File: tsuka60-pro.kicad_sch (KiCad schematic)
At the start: 166 parts, among them J1 USB_C_Receptacle_USB2.0, J2 Conn_01x04_MountingPin, SW1 SW_Reset, U1 ATmega32U4-M, U2 SRV05-4, Y1 16MHz

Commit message: Made important changes to the keyboard, re-exported production files
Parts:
- added MX70_2: MX-NoLED, marbastlib-mx:SW_MX_HS_1u, symbol MX_Alps_Hybrid:MX-NoLED
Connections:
- net COL9: now also MX70.1 (COL), MX70_2.1 (COL)
- net 70_2: now reaches D70.2 (A), MX70.2 (ROW)
- net 70_2: now also MX70_2.2 (ROW)
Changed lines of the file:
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@@
   (junction (at 166.37 138.43) (diameter 0) (color 0 0 0 0)
   )
+  (junction (at 171.45 166.37) (diameter 0) (color 0 0 0 0)
+  )
   (junction (at 82.55 90.17) (diameter 0) (color 0 0 0 0)
   )
@@
     (stroke (width 0) (type default) (color 0 0 0 0))
   )
+  (wire (pts (xy 171.45 166.37) (xy 171.45 204.47))
+    (stroke (width 0) (type default) (color 0 0 0 0))
+  )
   (wire (pts (xy 102.87 62.23) (xy 90.17 62.23))
     (stroke (width 0) (type default) (color 0 0 0 0))
@@
     )
   )
+  (global_label "70_2" (shape input) (at 179.07 260.35 180) (fields_autoplaced)
+    (effects (font (size 1.27 1.27)) (justify right))
+    (property "Intersheet References" "${INTERSHEET_REFS}" (id 0) (at 172.0607 260.2706 0)
+      (effects (font (size 1.27 1.27)) (justify right) hide)
+    )
+  )
   (global_label "COL11" (shape input) (at 370.84 53.34 0) (fields_autoplaced)
     (effects (font (size 1.27 1.27)) (justify left))
@@
     )
   )
+  (global_label "70_2" (shape input) (at 166.37 209.55 180) (fields_autoplaced)
+    (effects (font (size 1.27 1.27)) (justify right))
+    (property "Intersheet References" "${INTERSHEET_REFS}" (id 0) (at 159.3607 209.4706 0)
+      (effects (font (size 1.27 1.27)) (justify right) hide)
+    )
+  )
   (global_label "COL6" (shape input) (at 370.84 73.66 0) (fields_autoplaced)
     (effects (font (size 1.27 1.27)) (justify left))
@@
     )
   )
+  (global_label "COL9" (shape input) (at 184.15 255.27 270) (fields_autoplaced)
+    (effects (font (size 1.27 1.27)) (justify right))
+    (property "Intersheet References" "${INTERSHEET_REFS}" (id 0) (at 184.0706 262.5212 90)
+      (effects (font (size 1.27 1.27)) (justify right) hide)
+    )
+  )
   (global_label "XTAL1" (shape input) (at 304.8 76.2 0) (fields_autoplaced)
     (effects (font (size 1.27 1.27)) (justify left))
@@
     (pin "2")
   )
+  (symbol (lib_id "MX_Alps_Hybrid:MX-NoLED") (at 180.34 256.54 0) (unit 1)
+    (in_bom yes) (on_board yes) (fields_autoplaced)
+    (property "Reference" "MX70_2" (id 0) (at 181.2256 250.19 0)
+      (effects (font (size 1.524 1.524)))
+    )
+    (property "Value" "MX-NoLED" (id 1) (at 181.2256 251.46 0)
+      (effects (font (size 0.508 0.508)))
+    )
+    (property "Footprint" "marbastlib-mx:SW_MX_HS_1u" (id 2) (at 164.465 257.175 0)
+      (effects (font (size 1.524 1.524)) hide)
+    )
+    (property "Datasheet" "" (id 3) (at 164.465 257.175 0)
+      (effects (font (size 1.524 1.524)) hide)
+    )
+    (pin "1")
+    (pin "2")
+  )
   (symbol (lib_id "Device:D_Small") (at 77.47 212.09 90) (unit 1)
     (in_bom yes) (on_board yes)
@@
       (reference "MX70") (unit 1) (value "MX-NoLED") (footprint "marbastlib-mx:SW_MX_HS_1.25u")
     )
+    (path "/834bb16e-2315-416c-95af-99912f2fa973"
+      (reference "MX70_2") (unit 1) (value "MX-NoLED") (footprint "marbastlib-mx:SW_MX_HS_1u")
+    )
     (path "/2db2779d-a5fd-464e-b5ae-8e46bd29d16e"

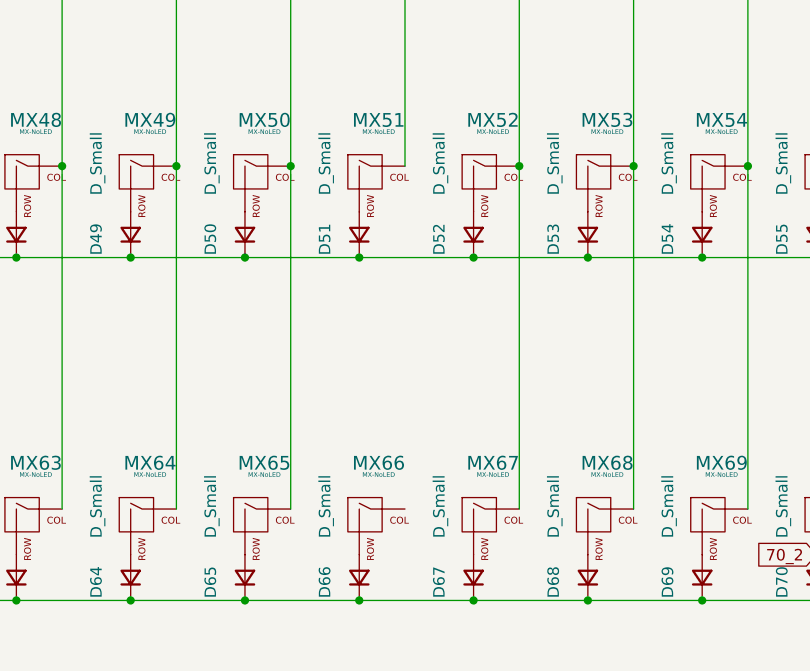
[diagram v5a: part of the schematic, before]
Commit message: Add missing trace
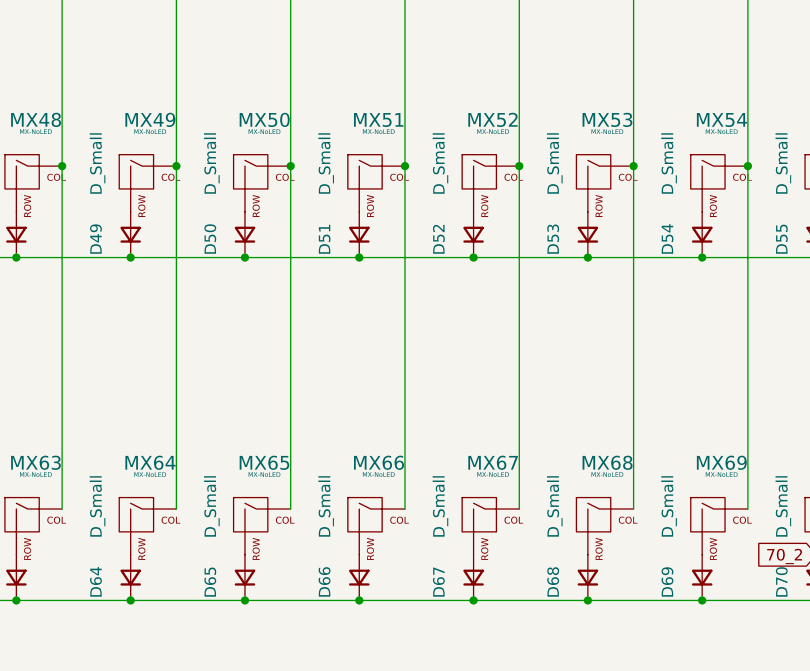
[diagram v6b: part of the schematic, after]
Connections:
- net COL5: now also MX66.1 (COL)
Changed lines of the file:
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@@
   (junction (at 289.56 85.09) (diameter 0) (color 0 0 0 0)
+  )
+  (junction (at 120.65 166.37) (diameter 0) (color 0 0 0 0)
   )
   (junction (at 115.57 176.53) (diameter 0) (color 0 0 0 0)
@@
     (stroke (width 0) (type default) (color 0 0 0 0))
   )
+  (wire (pts (xy 120.65 166.37) (xy 120.65 204.47))
+    (stroke (width 0) (type default) (color 0 0 0 0))
+  )

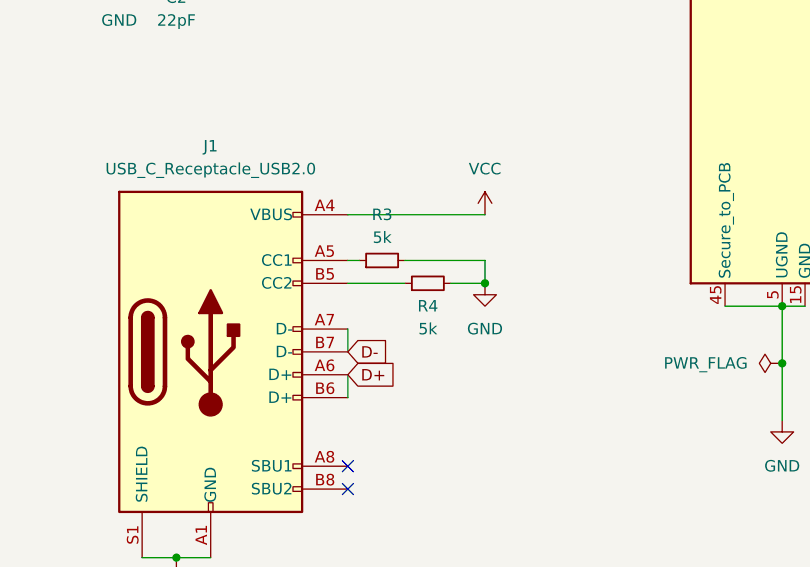
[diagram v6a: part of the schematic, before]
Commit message: Repair BOM, update USB-C component, footprint and placement
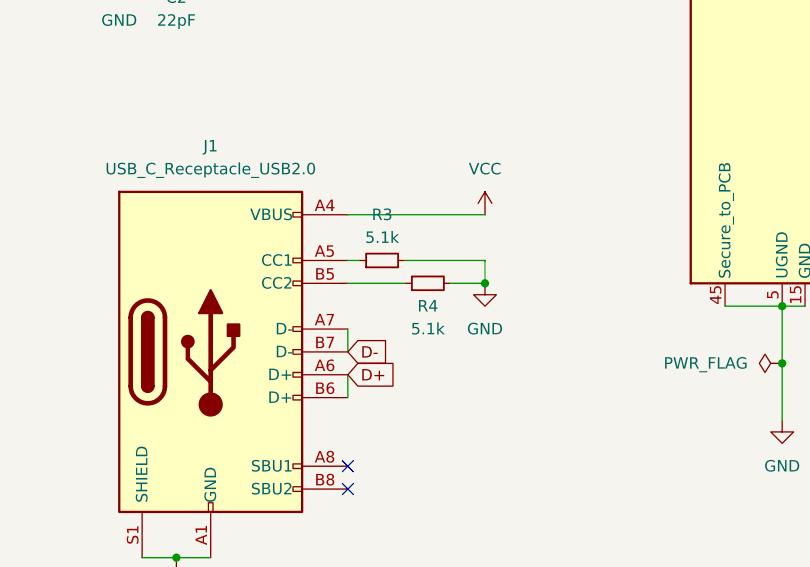
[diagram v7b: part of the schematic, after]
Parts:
- J1: footprint marbastlib-various:USB_C_Receptacle_HRO_TYPE-C-31-M-14 -> Connector_USB:USB_C_Receptacle_HRO_TYPE-C-31-M-12
- R3, R4: value 5k -> 5.1k
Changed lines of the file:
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@@
     (property "Reference" "J1" (id 0) (at 289.56 109.22 0))
     (property "Value" "USB_C_Receptacle_USB2.0" (id 1) (at 289.56 111.76 0))
-    (property "Footprint" "marbastlib-various:USB_C_Receptacle_HRO_TYPE-C-31-M-14" (id 2) (at 293.37 132.08 0)
+    (property "Footprint" "Connector_USB:USB_C_Receptacle_HRO_TYPE-C-31-M-12" (id 2) (at 293.37 132.08 0)
       (effects (font (size 1.27 1.27)) hide)
     )
@@
     (in_bom yes) (on_board yes)
     (property "Reference" "R4" (id 0) (at 313.69 127 90))
-    (property "Value" "5k" (id 1) (at 313.69 129.54 90))
+    (property "Value" "5.1k" (id 1) (at 313.69 129.54 90))
     (property "Footprint" "Capacitor_SMD:C_0603_1608Metric_Pad1.08x0.95mm_HandSolder" (id 2) (at 313.69 124.46 0)
       (effects (font (size 1.27 1.27)) hide)
@@
     (in_bom yes) (on_board yes)
     (property "Reference" "R3" (id 0) (at 308.61 116.84 90))
-    (property "Value" "5k" (id 1) (at 308.61 119.38 90))
+    (property "Value" "5.1k" (id 1) (at 308.61 119.38 90))
     (property "Footprint" "Capacitor_SMD:C_0603_1608Metric_Pad1.08x0.95mm_HandSolder" (id 2) (at 308.61 121.92 0)
       (effects (font (size 1.27 1.27)) hide)
@@
     )
     (path "/39fd6eec-df64-4ec7-90d9-dff965db8c15"
-      (reference "J1") (unit 1) (value "USB_C_Receptacle_USB2.0") (footprint "marbastlib-various:USB_C_Receptacle_HRO_TYPE-C-31-M-14")
+      (reference "J1") (unit 1) (value "USB_C_Receptacle_USB2.0") (footprint "Connector_USB:USB_C_Receptacle_HRO_TYPE-C-31-M-12")
     )
     (path "/08e6d373-2bf3-4f1e-87e0-beb65fb65c5f"
@@
     )
     (path "/65a31d27-e55c-4cca-9abe-ecfeb4877455"
-      (reference "R3") (unit 1) (value "5k") (footprint "Capacitor_SMD:C_0603_1608Metric_Pad1.08x0.95mm_HandSolder")
+      (reference "R3") (unit 1) (value "5.1k") (footprint "Capacitor_SMD:C_0603_1608Metric_Pad1.08x0.95mm_HandSolder")
     )
     (path "/542c3b37-d462-4e93-9988-5091b5e59bf5"
-      (reference "R4") (unit 1) (value "5k") (footprint "Capacitor_SMD:C_0603_1608Metric_Pad1.08x0.95mm_HandSolder")
+      (reference "R4") (unit 1) (value "5.1k") (footprint "Capacitor_SMD:C_0603_1608Metric_Pad1.08x0.95mm_HandSolder")
     )
     (path "/276330b8-e138-464f-8b38-13c9c7f3efbd"

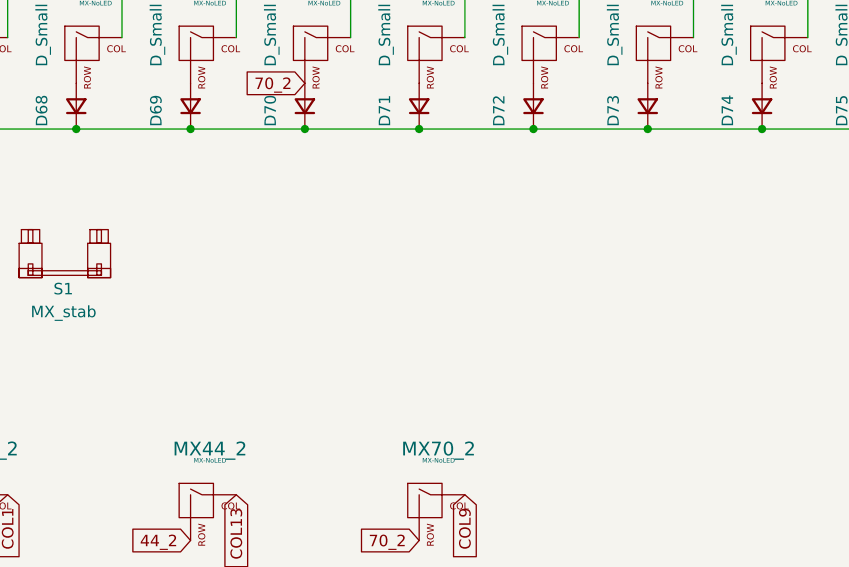
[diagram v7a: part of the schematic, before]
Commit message: Add mounting holes and re-export productions files
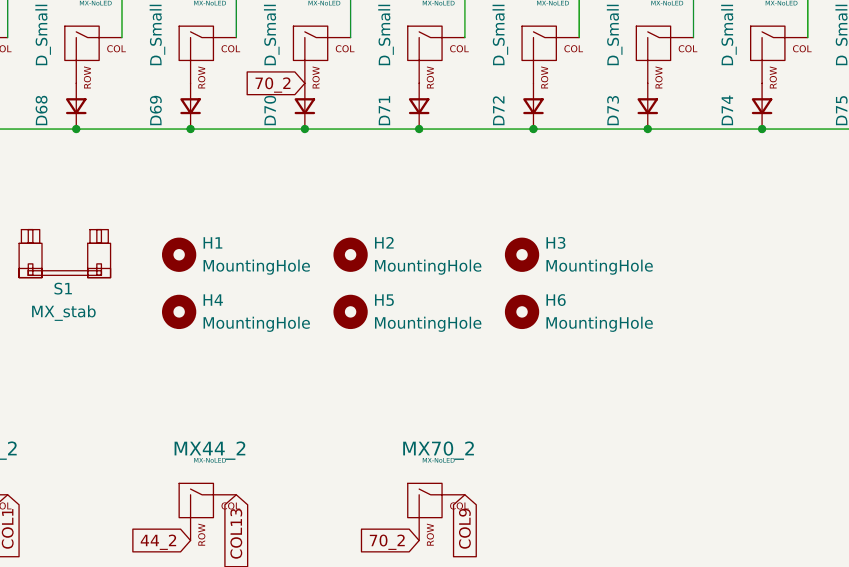
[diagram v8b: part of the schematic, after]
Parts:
- added H1, H2, H3, H4, H5, H6: MountingHole, MountingHole:MountingHole_2.2mm_M2_Pad_TopOnly, symbol Mechanical:MountingHole
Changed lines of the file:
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@@
     (pin "2")
+  )
+  (symbol (lib_id "Mechanical:MountingHole") (at 190.5 234.95 0) (unit 1)
+    (in_bom yes) (on_board yes) (fields_autoplaced)
+    (property "Reference" "H6" (id 0) (at 193.04 233.6799 0)
+      (effects (font (size 1.27 1.27)) (justify left))
+    )
+    (property "Value" "MountingHole" (id 1) (at 193.04 236.2199 0)
+      (effects (font (size 1.27 1.27)) (justify left))
+    )
+    (property "Footprint" "MountingHole:MountingHole_2.2mm_M2_Pad_TopOnly" (id 2) (at 190.5 234.95 0)
+      (effects (font (size 1.27 1.27)) hide)
+    )
+    (property "Datasheet" "~" (id 3) (at 190.5 234.95 0)
+      (effects (font (size 1.27 1.27)) hide)
+    )
   )
   (symbol (lib_id "Connector:USB_C_Receptacle_USB2.0") (at 289.56 132.08 0) (unit 1)
@@
     )
     (pin "1")
+  )
+  (symbol (lib_id "Mechanical:MountingHole") (at 190.5 228.6 0) (unit 1)
+    (in_bom yes) (on_board yes) (fields_autoplaced)
+    (property "Reference" "H3" (id 0) (at 193.04 227.3299 0)
+      (effects (font (size 1.27 1.27)) (justify left))
+    )
+    (property "Value" "MountingHole" (id 1) (at 193.04 229.8699 0)
+      (effects (font (size 1.27 1.27)) (justify left))
+    )
+    (property "Footprint" "MountingHole:MountingHole_2.2mm_M2_Pad_TopOnly" (id 2) (at 190.5 228.6 0)
+      (effects (font (size 1.27 1.27)) hide)
+    )
+    (property "Datasheet" "~" (id 3) (at 190.5 228.6 0)
+      (effects (font (size 1.27 1.27)) hide)
+    )
   )
   (symbol (lib_id "MX_Alps_Hybrid:MX-NoLED") (at 53.34 205.74 0) (unit 1)
@@
     (pin "2")
   )
+  (symbol (lib_id "Mechanical:MountingHole") (at 171.45 228.6 0) (unit 1)
+    (in_bom yes) (on_board yes) (fields_autoplaced)
+    (property "Reference" "H2" (id 0) (at 173.99 227.3299 0)
+      (effects (font (size 1.27 1.27)) (justify left))
+    )
+    (property "Value" "MountingHole" (id 1) (at 173.99 229.8699 0)
+      (effects (font (size 1.27 1.27)) (justify left))
+    )
+    (property "Footprint" "MountingHole:MountingHole_2.2mm_M2_Pad_TopOnly" (id 2) (at 171.45 228.6 0)
+      (effects (font (size 1.27 1.27)) hide)
+    )
+    (property "Datasheet" "~" (id 3) (at 171.45 228.6 0)
+      (effects (font (size 1.27 1.27)) hide)
+    )
+  )
   (symbol (lib_id "MX_Alps_Hybrid:MX-NoLED") (at 78.74 167.64 0) (unit 1)
     (in_bom yes) (on_board yes) (fields_autoplaced)
@@
     (pin "2")
   )
+  (symbol (lib_id "Mechanical:MountingHole") (at 152.4 228.6 0) (unit 1)
+    (in_bom yes) (on_board yes) (fields_autoplaced)
+    (property "Reference" "H1" (id 0) (at 154.94 227.3299 0)
+      (effects (font (size 1.27 1.27)) (justify left))
+    )
+    (property "Value" "MountingHole" (id 1) (at 154.94 229.8699 0)
+      (effects (font (size 1.27 1.27)) (justify left))
+    )
+    (property "Footprint" "MountingHole:MountingHole_2.2mm_M2_Pad_TopOnly" (id 2) (at 152.4 228.6 0)
+      (effects (font (size 1.27 1.27)) hide)
+    )
+    (property "Datasheet" "~" (id 3) (at 152.4 228.6 0)
+      (effects (font (size 1.27 1.27)) hide)
+    )
+  )
+  (symbol (lib_id "Mechanical:MountingHole") (at 152.4 234.95 0) (unit 1)
+    (in_bom yes) (on_board yes) (fields_autoplaced)
+    (property "Reference" "H4" (id 0) (at 154.94 233.6799 0)
+      (effects (font (size 1.27 1.27)) (justify left))
+    )
+    (property "Value" "MountingHole" (id 1) (at 154.94 236.2199 0)
+      (effects (font (size 1.27 1.27)) (justify left))
+    )
+    (property "Footprint" "MountingHole:MountingHole_2.2mm_M2_Pad_TopOnly" (id 2) (at 152.4 234.95 0)
+      (effects (font (size 1.27 1.27)) hide)
+    )
+    (property "Datasheet" "~" (id 3) (at 152.4 234.95 0)
+      (effects (font (size 1.27 1.27)) hide)
+    )
+  )
   (symbol (lib_id "Device:D_Small") (at 191.77 59.69 90) (unit 1)
     (in_bom yes) (on_board yes)
@@
     (pin "2")
   )
+  (symbol (lib_id "Mechanical:MountingHole") (at 171.45 234.95 0) (unit 1)
+    (in_bom yes) (on_board yes) (fields_autoplaced)
+    (property "Reference" "H5" (id 0) (at 173.99 233.6799 0)
+      (effects (font (size 1.27 1.27)) (justify left))
+    )
+    (property "Value" "MountingHole" (id 1) (at 173.99 236.2199 0)
+      (effects (font (size 1.27 1.27)) (justify left))
+    )
+    (property "Footprint" "MountingHole:MountingHole_2.2mm_M2_Pad_TopOnly" (id 2) (at 171.45 234.95 0)
+      (effects (font (size 1.27 1.27)) hide)
+    )
+    (property "Datasheet" "~" (id 3) (at 171.45 234.95 0)
+      (effects (font (size 1.27 1.27)) hide)
+    )
+  )
   (symbol (lib_id "Device:D_Small") (at 140.97 59.69 90) (unit 1)
     (in_bom yes) (on_board yes)
@@
       (reference "F1") (unit 1) (value "500mA") (footprint "Fuse:Fuse_1206_3216Metric_Pad1.42x1.75mm_HandSolder")
     )
+    (path "/c87db475-66df-412f-aca4-d770d65190d4"
+      (reference "H1") (unit 1) (value "MountingHole") (footprint "MountingHole:MountingHole_2.2mm_M2_Pad_TopOnly")
+    )
+    (path "/b80c4215-83b2-4780-8536-3e4a81cb3e69"
+      (reference "H2") (unit 1) (value "MountingHole") (footprint "MountingHole:MountingHole_2.2mm_M2_Pad_TopOnly")
+    )
+    (path "/4855c882-bf2b-42b9-8749-fdf24f521454"
+      (reference "H3") (unit 1) (value "MountingHole") (footprint "MountingHole:MountingHole_2.2mm_M2_Pad_TopOnly")
+    )
+    (path "/ca641664-7f59-444b-a012-371fd18f0c2b"
+      (reference "H4") (unit 1) (value "MountingHole") (footprint "MountingHole:MountingHole_2.2mm_M2_Pad_TopOnly")
+    )
+    (path "/e41b6d36-5342-4fb8-a35f-6225027ad06e"
+      (reference "H5") (unit 1) (value "MountingHole") (footprint "MountingHole:MountingHole_2.2mm_M2_Pad_TopOnly")
+    )
+    (path "/387bddf3-78fe-4cce-ae21-39f896d21f93"
+      (reference "H6") (unit 1) (value "MountingHole") (footprint "MountingHole:MountingHole_2.2mm_M2_Pad_TopOnly")
+    )
     (path "/39fd6eec-df64-4ec7-90d9-dff965db8c15"
